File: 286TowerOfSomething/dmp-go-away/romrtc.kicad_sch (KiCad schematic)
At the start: 1 part, among them U1 M6117C

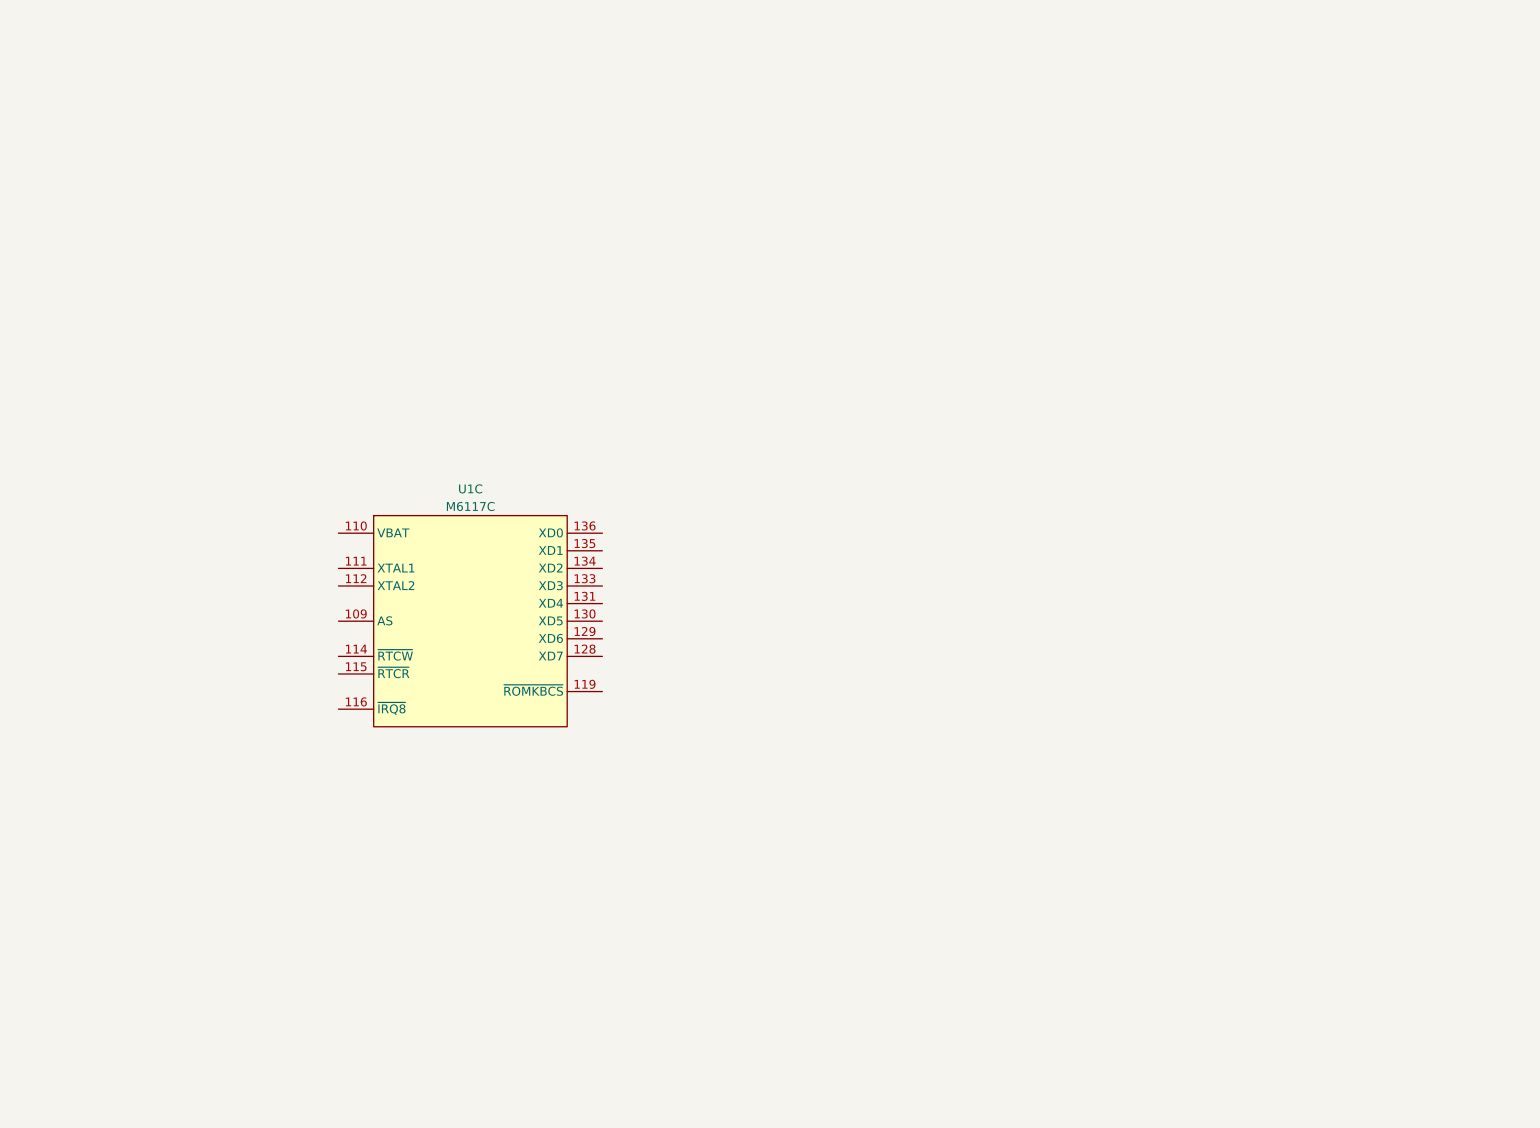
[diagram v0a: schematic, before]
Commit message: Adding work done on 386 card, coming along nicely
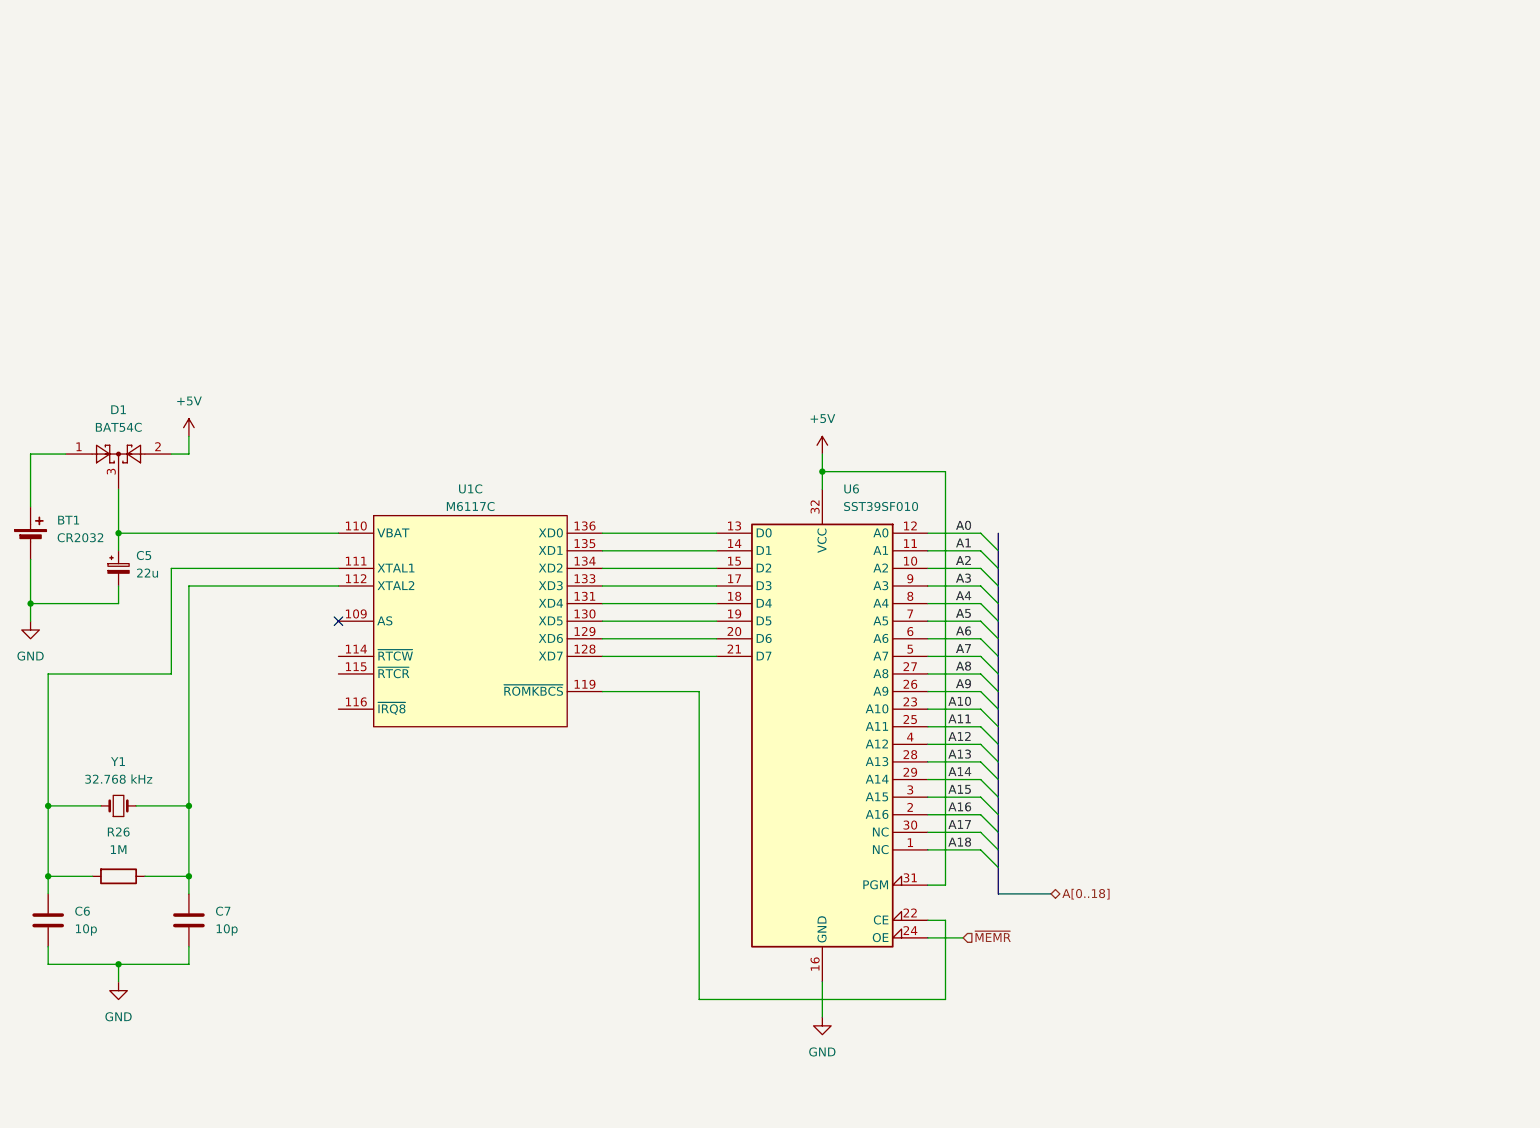
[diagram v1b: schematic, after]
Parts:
- added BT1: CR2032, symbol Device:Battery_Cell
- added C5: 22u, symbol Device:C_Polarized_Small
- added C6, C7: 10p, symbol Device:C
- added D1: BAT54C, Package_TO_SOT_SMD:SOT-23, symbol Diode:BAT54C
- added R26: 1M, symbol Device:R
- added U6: SST39SF010, symbol Memory_Flash:SST39SF010
- added Y1: 32.768 kHz, symbol Device:Crystal_Small
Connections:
- net at U1.110 (VBAT): now also C5.1, D1.3
- net at U1.111 (XTAL1): now also C6.1, R26.2, Y1.1
- net at U1.112 (XTAL2): now also C7.1, R26.1, Y1.2
- net at U1.119 (~{ROMKBCS}): now also U6.22 (CE)
- net at U1.128 (XD7): now also U6.21 (D7)
- net at U1.129 (XD6): now also U6.20 (D6)
- net at U1.130 (XD5): now also U6.19 (D5)
- net at U1.131 (XD4): now also U6.18 (D4)
- net at U1.133 (XD3): now also U6.17 (D3)
- net at U1.134 (XD2): now also U6.15 (D2)
- net at U1.135 (XD1): now also U6.14 (D1)
- net at U1.136 (XD0): now also U6.13 (D0)
- new net: BT1.1 (+), D1.1
- new net +5V: D1.2, U6.31 (PGM), U6.32 (VCC)
- new net A0: U6.12 (A0)
- new net A1: U6.11 (A1)
- new net A10: U6.23 (A10)
- new net A11: U6.25 (A11)
- new net A12: U6.4 (A12)
- new net A13: U6.28 (A13)
- new net A14: U6.29 (A14)
- new net A15: U6.3 (A15)
- new net A16: U6.2 (A16)
- new net A17: U6.30 (NC)
- new net A18: U6.1 (NC)
- new net A2: U6.10 (A2)
- new net A3: U6.9 (A3)
- new net A4: U6.8 (A4)
- new net A5: U6.7 (A5)
- new net A6: U6.6 (A6)
- new net A7: U6.5 (A7)
- new net A8: U6.27 (A8)
- new net A9: U6.26 (A9)
- new net GND: BT1.2 (-), C5.2, C6.2, C7.2, U6.16 (GND)
- new net ~{MEMR}: U6.24 (OE)
- no-connect marks 0 -> 1

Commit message: Adding some missing caps, and the optional DS12885 RTC for dmp-go-away
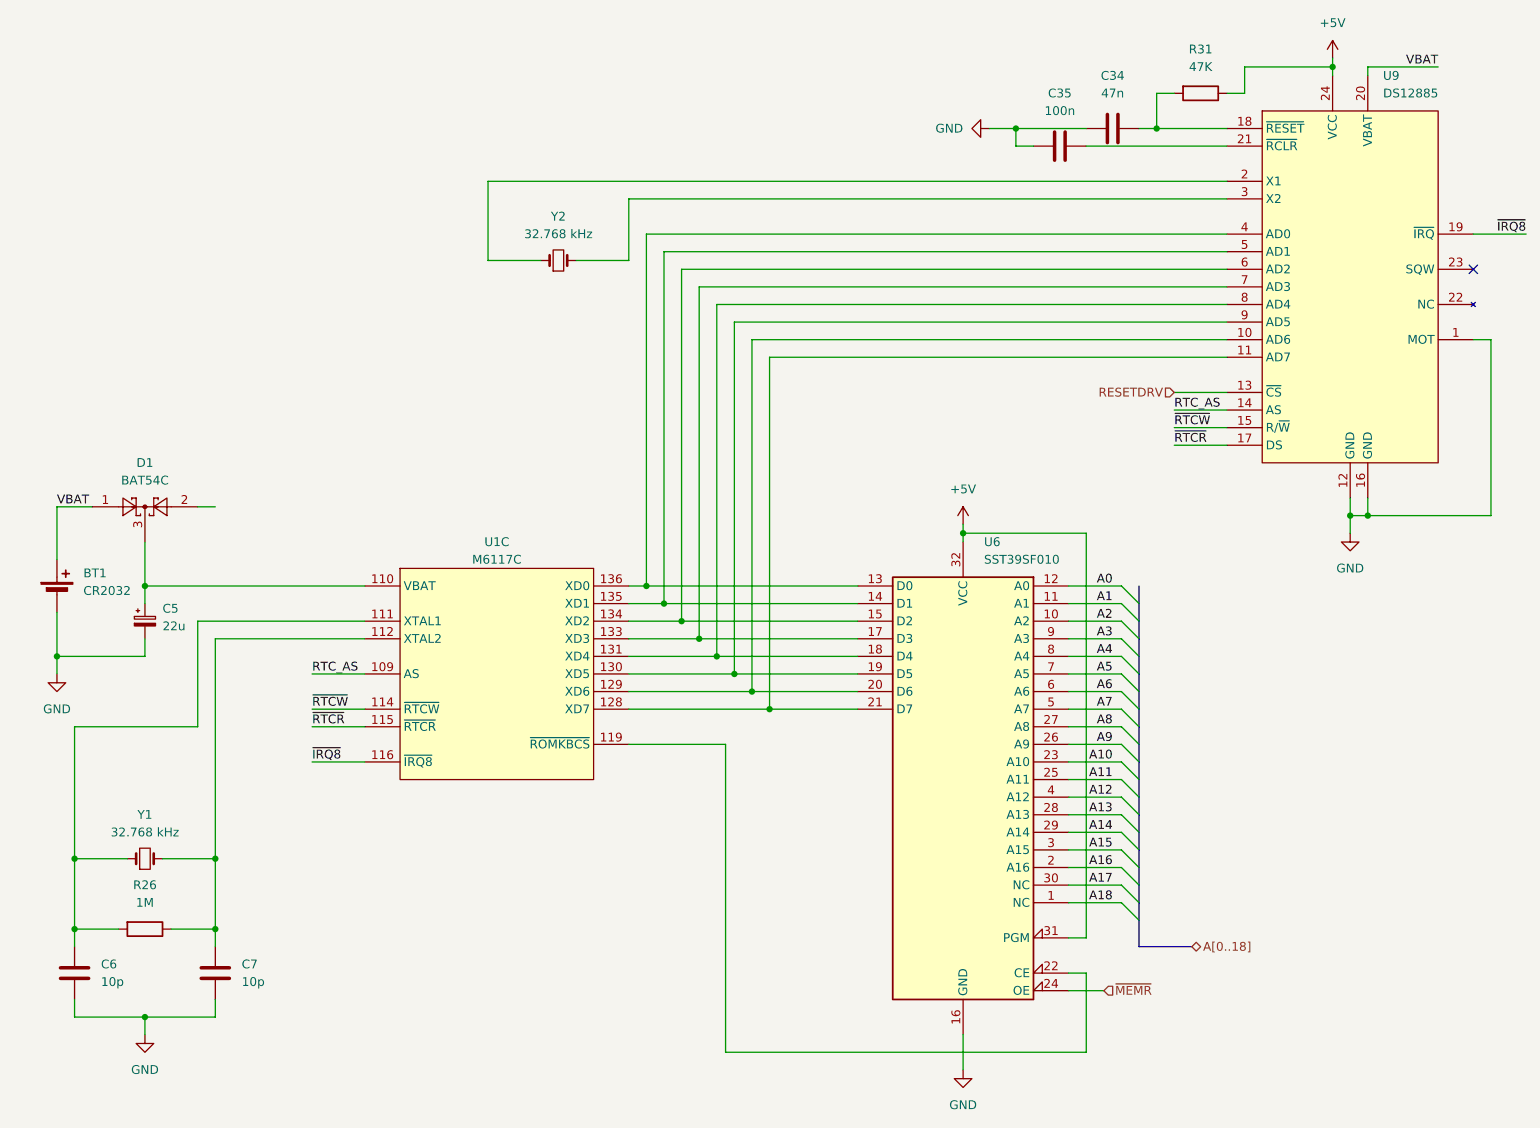
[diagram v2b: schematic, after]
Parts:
- added C34: 47n, symbol Device:C
- added C35: 100n, symbol Device:C
- added R31: 47K, symbol Device:R
- added U9: DS12885, Package_DIP:DIP-24_W15.24mm, symbol pc-parts:DS12885
- added Y2: 32.768 kHz, symbol Device:Crystal_Small
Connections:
- net +5V: now also R31.1, U9.24 (VCC); no longer D1.2
- net GND: now also C34.2, C35.2, U9.1 (MOT), U9.12 (GND), U9.16 (GND)
- net VBAT: now reaches BT1.1 (+), D1.1
- net VBAT: now also U9.20 (VBAT)
- net at U1.136 (XD0), U6.13 (D0): now also U9.4 (AD0)
- net at U1.135 (XD1), U6.14 (D1): now also U9.5 (AD1)
- net at U1.134 (XD2), U6.15 (D2): now also U9.6 (AD2)
- net at U1.133 (XD3), U6.17 (D3): now also U9.7 (AD3)
- net at U1.131 (XD4), U6.18 (D4): now also U9.8 (AD4)
- net at U1.130 (XD5), U6.19 (D5): now also U9.9 (AD5)
- net at U1.129 (XD6), U6.20 (D6): now also U9.10 (AD6)
- net at U1.128 (XD7), U6.21 (D7): now also U9.11 (AD7)
- net RTC_AS: now reaches U1.109 (AS)
- net RTC_AS: now also U9.14 (AS)
- net ~{RTCW}: now reaches U1.114 (~{RTCW})
- net ~{RTCW}: now also U9.15 (R/~{W})
- net ~{RTCR}: now reaches U1.115 (~{RTCR})
- net ~{RTCR}: now also U9.17 (DS)
- net ~{IRQ8}: now reaches U1.116 (~{IRQ8})
- net ~{IRQ8}: now also U9.19 (~{IRQ})
- new net: C34.1, R31.2, U9.18 (~{RESET})
- new net: U9.2 (X1), Y2.1
- new net: U9.3 (X2), Y2.2
- new net: C35.1, U9.21 (~{RCLR})
- new net RESETDRV: U9.13 (~{CS})
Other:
- moved on the sheet: BT1, C5, C6, C7, D1, R26, U1C, U6, Y1

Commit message: Added footprints and started figuring out layout for dmp-go-away
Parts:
- BT1: footprint (none) -> Battery:BatteryHolder_Keystone_1060_1x2032
- C34, C35, C6, C7: footprint (none) -> Capacitor_SMD:C_0603_1608Metric_Pad1.08x0.95mm_HandSolder
- C5: footprint (none) -> Capacitor_SMD:CP_Elec_5x5.3
- R26, R31: footprint (none) -> Resistor_SMD:R_0603_1608Metric_Pad0.98x0.95mm_HandSolder
- U1: footprint (none) -> Package_QFP:PQFP-208_28x28mm_P0.5mm
- U6: footprint (none) -> Package_DIP:DIP-32_W15.24mm_Socket
- Y1, Y2: footprint (none) -> Crystal:Crystal_AT310_D3.0mm_L10.0mm_Vertical
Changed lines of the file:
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@@
 			)
 		)
-		(property "Footprint" ""
+		(property "Footprint" "Capacitor_SMD:C_0603_1608Metric_Pad1.08x0.95mm_HandSolder"
 			(at 190.5 30.1752 0)
 			(effects
@@
 			)
 		)
-		(property "Footprint" ""
+		(property "Footprint" "Crystal:Crystal_AT310_D3.0mm_L10.0mm_Vertical"
 			(at 114.3 48.26 0)
 			(effects
@@
 			)
 		)
-		(property "Footprint" ""
+		(property "Footprint" "Capacitor_SMD:C_0603_1608Metric_Pad1.08x0.95mm_HandSolder"
 			(at 45.4152 154.94 0)
 			(effects
@@
 			)
 		)
-		(property "Footprint" ""
+		(property "Footprint" "Resistor_SMD:R_0603_1608Metric_Pad0.98x0.95mm_HandSolder"
 			(at 54.61 143.002 90)
 			(effects
@@
 			)
 		)
-		(property "Footprint" ""
+		(property "Footprint" "Crystal:Crystal_AT310_D3.0mm_L10.0mm_Vertical"
 			(at 54.61 134.62 0)
 			(effects
@@
 			)
 		)
-		(property "Footprint" ""
+		(property "Footprint" "Battery:BatteryHolder_Keystone_1060_1x2032"
 			(at 41.91 94.996 90)
 			(effects
@@
 			)
 		)
-		(property "Footprint" ""
+		(property "Footprint" "Capacitor_SMD:CP_Elec_5x5.3"
 			(at 54.61 100.33 0)
 			(effects
@@
 			)
 		)
-		(property "Footprint" ""
+		(property "Footprint" "Resistor_SMD:R_0603_1608Metric_Pad0.98x0.95mm_HandSolder"
 			(at 207.01 22.352 90)
 			(effects
@@
 			)
 		)
-		(property "Footprint" ""
+		(property "Footprint" "Capacitor_SMD:C_0603_1608Metric_Pad1.08x0.95mm_HandSolder"
 			(at 182.88 32.7152 0)
 			(effects
@@
 			)
 		)
-		(property "Footprint" ""
+		(property "Footprint" "Package_DIP:DIP-32_W15.24mm_Socket"
 			(at 172.72 118.11 0)
 			(effects
@@
 			)
 		)
-		(property "Footprint" ""
+		(property "Footprint" "Package_QFP:PQFP-208_28x28mm_P0.5mm"
 			(at 105.41 107.95 0)
 			(effects
@@
 			)
 		)
-		(property "Footprint" ""
+		(property "Footprint" "Capacitor_SMD:C_0603_1608Metric_Pad1.08x0.95mm_HandSolder"
 			(at 65.7352 154.94 0)
 			(effects
